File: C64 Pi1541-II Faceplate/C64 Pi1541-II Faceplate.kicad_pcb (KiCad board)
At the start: 2 copper layers, 97.8 x 97.8 mm, 9 parts, among them IC1 0.96_OLED, J4 Faceplate, M1 Mounting, M2 Mounting, M3 Mounting, M4 Mounting

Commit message: Added copper layer to backplate
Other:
- board text added: "PI1541-II Faceplate (rev. B) github.com/tebl Licensed under CERN OHL v.1.2"
- board text removed: "PI1541-II Faceplate github.com/tebl Licensed under CERN OHL v.1.2"
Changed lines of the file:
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@@
     (descr "Through hole straight pin header, 1x04, 2.54mm pitch, single row")
     (tags "Through hole pin header THT 1x04 2.54mm single row")
-    (fp_text reference J4 (at 0 3.175 90) (layer B.SilkS)
-      (effects (font (size 1 1) (thickness 0.15)) (justify mirror))
-    )
-    (fp_text value Faceplate (at 2.54 -3.81 90) (layer B.Fab)
+    (fp_text reference J4 (at -2.54 0 90) (layer B.SilkS)
+      (effects (font (size 1 1) (thickness 0.15)) (justify mirror))
+    )
+    (fp_text value Faceplate (at -2.54 -5.08 90) (layer B.SilkS)
       (effects (font (size 1 1) (thickness 0.15)) (justify mirror))
     )
@@
   (gr_line (start 120.65 62.23) (end 120.65 78.105) (layer Edge.Cuts) (width 0.15))
   (gr_line (start 95.25 62.23) (end 120.65 62.23) (layer Edge.Cuts) (width 0.15))
-  (gr_text "PI1541-II Faceplate\ngithub.com/tebl\n\nLicensed under\nCERN OHL v.1.2" (at 142.24 78.105) (layer B.SilkS)
+  (gr_text "PI1541-II\nFaceplate (rev. B)\ngithub.com/tebl\n\nLicensed under\nCERN OHL v.1.2" (at 142.24 78.105) (layer B.SilkS)
     (effects (font (size 1.5 1.5) (thickness 0.15)) (justify mirror))
   )

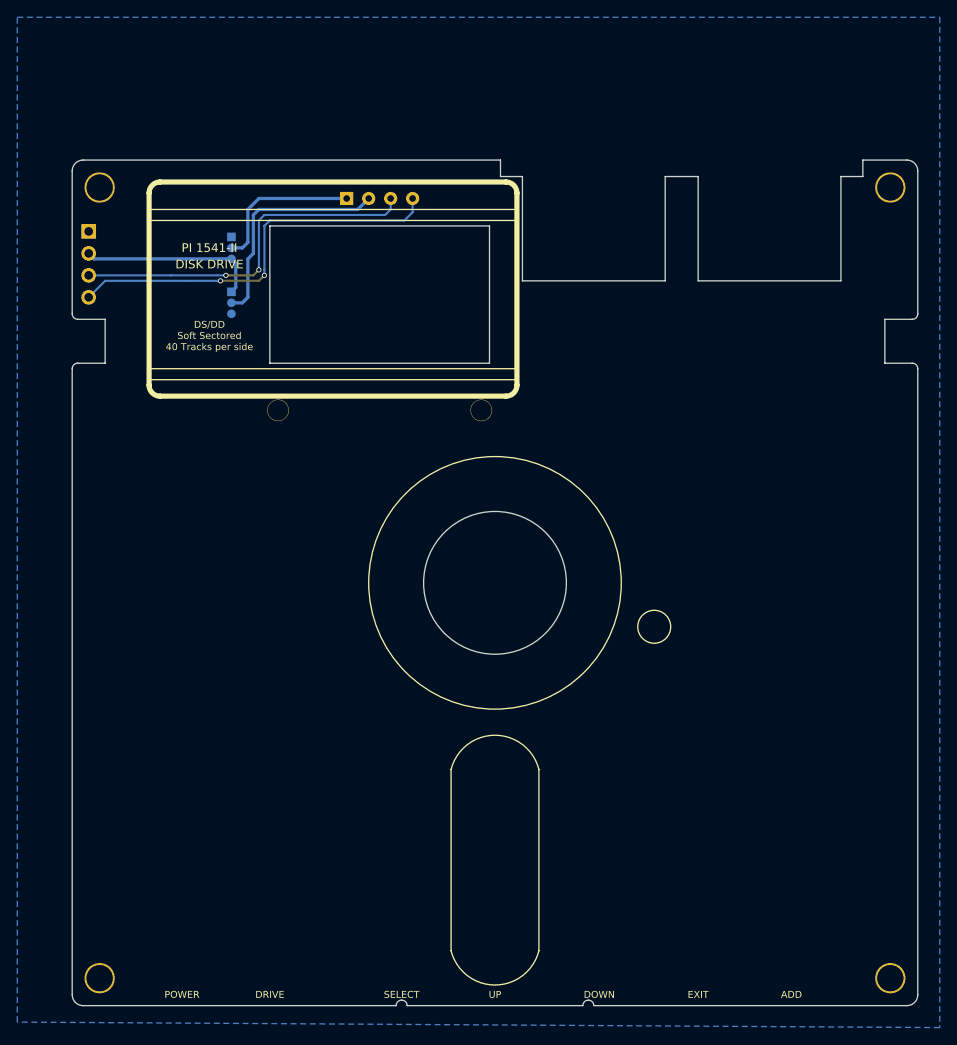
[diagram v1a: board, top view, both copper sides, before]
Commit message: Tweaked faceplate cutouts
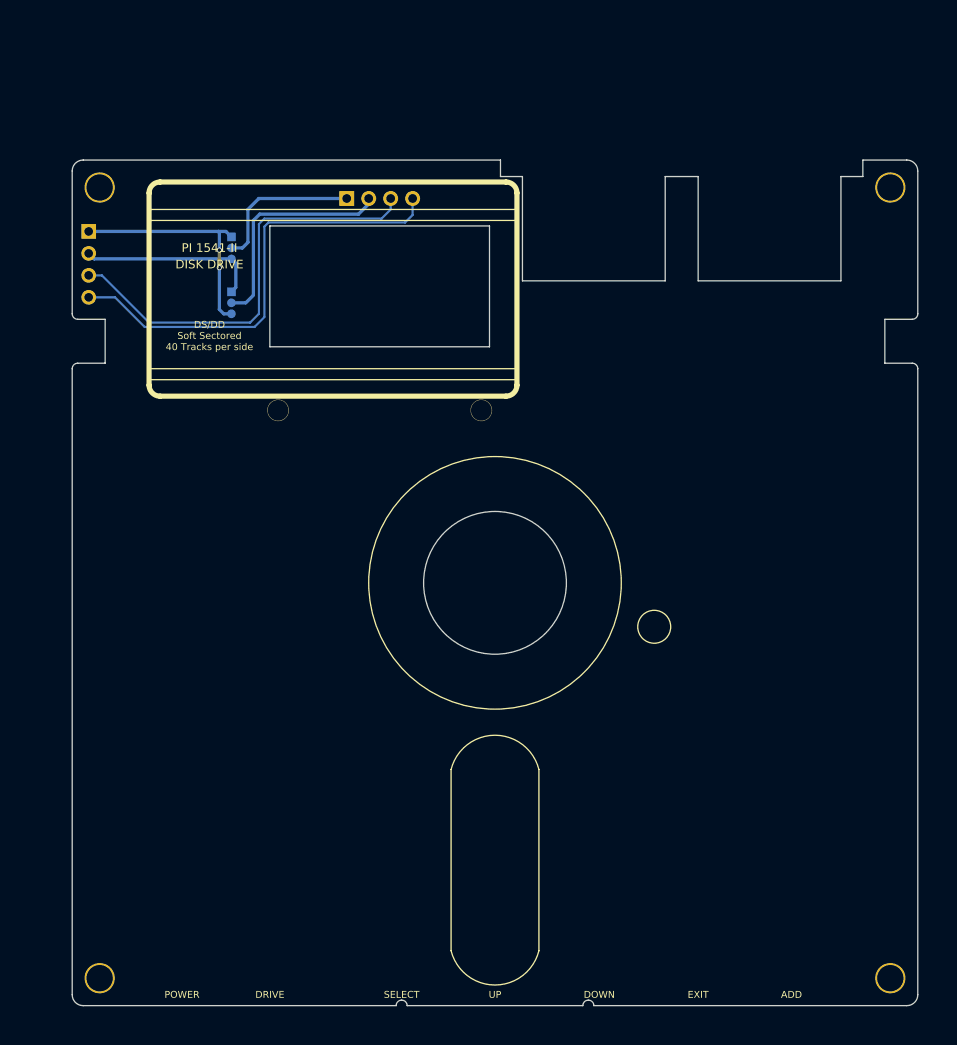
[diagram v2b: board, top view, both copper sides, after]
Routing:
- net GND: track 0.00 -> 27.5 mm, vias 0 -> 2
- net I2C_SCL: track 43.3 -> 50.6 mm, vias 2 -> 0
- net I2C_SDA: track 46.5 -> 52.3 mm, vias 2 -> 0
- removed copper zone on B.Cu, net GND
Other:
- outline, holes or cut-outs redrawn
